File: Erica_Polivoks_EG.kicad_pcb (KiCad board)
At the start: 2 copper layers, 81.7 x 128.5 mm, 105 parts, among them J1 GATE IN, J2 INV EG OUT, J3 Eurorack_Power_10pin_Unshroud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, J4 GATE D.OUT, J5 EG OUT, Q1 4, Q2 4, Q3 4, Q4 4, Q5 4, Q6 4, Q7 6, Q8 6, Q9 6, U1 TL074

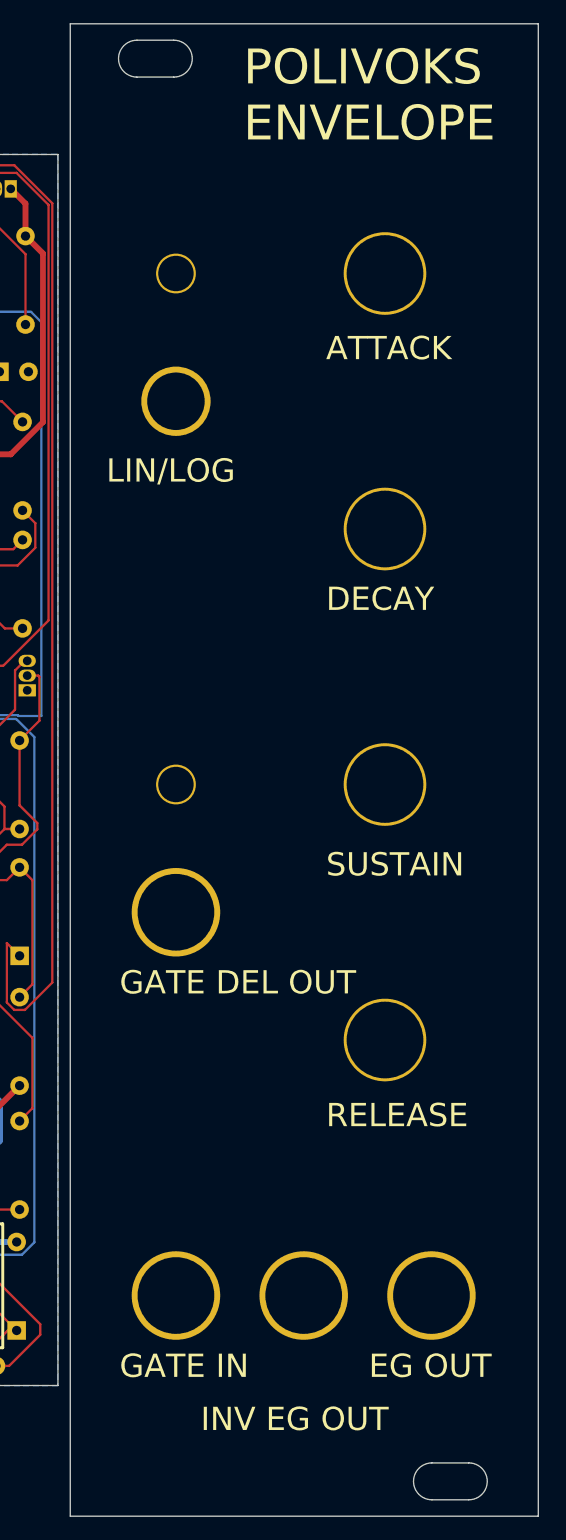
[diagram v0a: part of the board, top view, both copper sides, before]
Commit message: broke panel out into separate PCB file
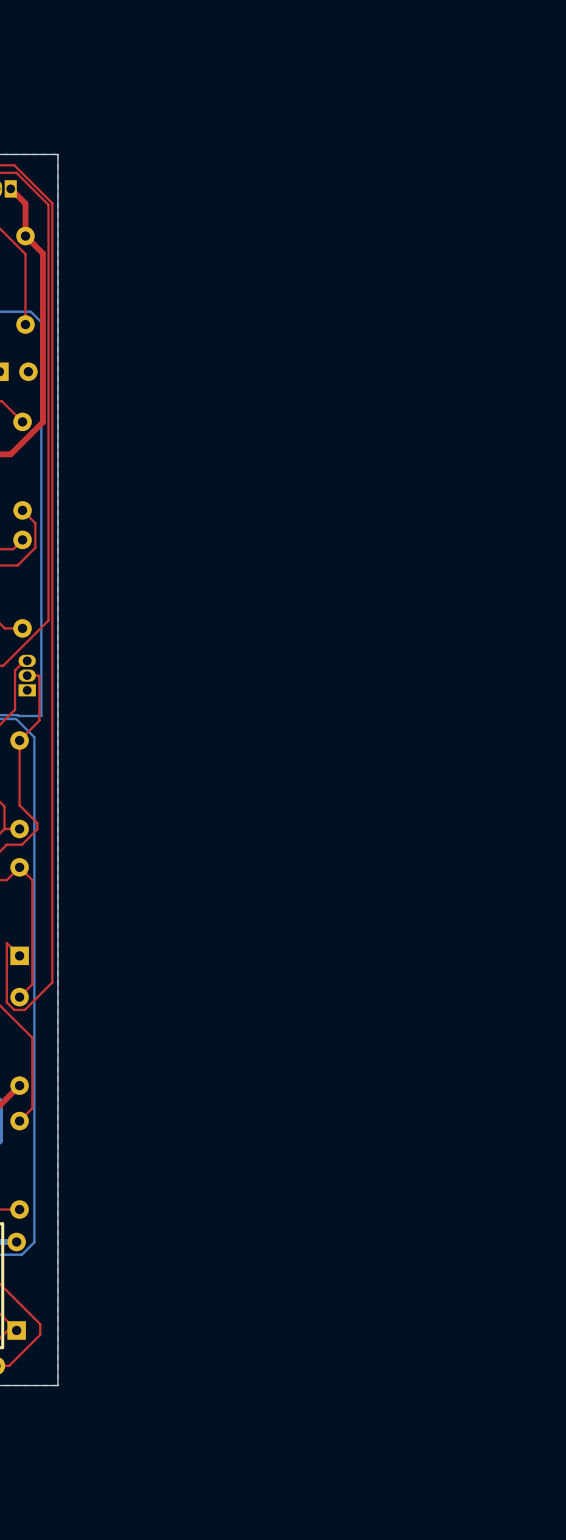
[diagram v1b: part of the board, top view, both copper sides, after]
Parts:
- removed REF** (x4): GND, PCM_4ms_Faceplate:Faceplate_Hole_Jack_3.5mm
- removed REF** (x2): Faceplate_Hole_LED_3mm, PCM_4ms_Faceplate:Faceplate_Hole_LED_3mm
- removed REF** (x4): Faceplate_Hole_Pot_9mm, PCM_4ms_Faceplate:Faceplate_Hole_Pot_9mm
- removed REF** (x2): Rail_mount_slot, PCM_4ms_Faceplate:Faceplate_Rail_Mount_Slot
- removed REF**: Faceplate_Hole_SubMini_Toggle, PCM_4ms_Faceplate:Faceplate_Hole_SubMini_Toggle
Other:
- board size 81.7 x 128.5 mm -> 40.3 x 106 mm
- board text removed: "EG OUT"
- board text removed: "GATE DEL OUT"
- board text removed: "GATE IN"
- board text removed: "INV EG OUT"
- board text removed: "LIN/LOG"
- board text removed: "POLIVOKS ENVELOPE"

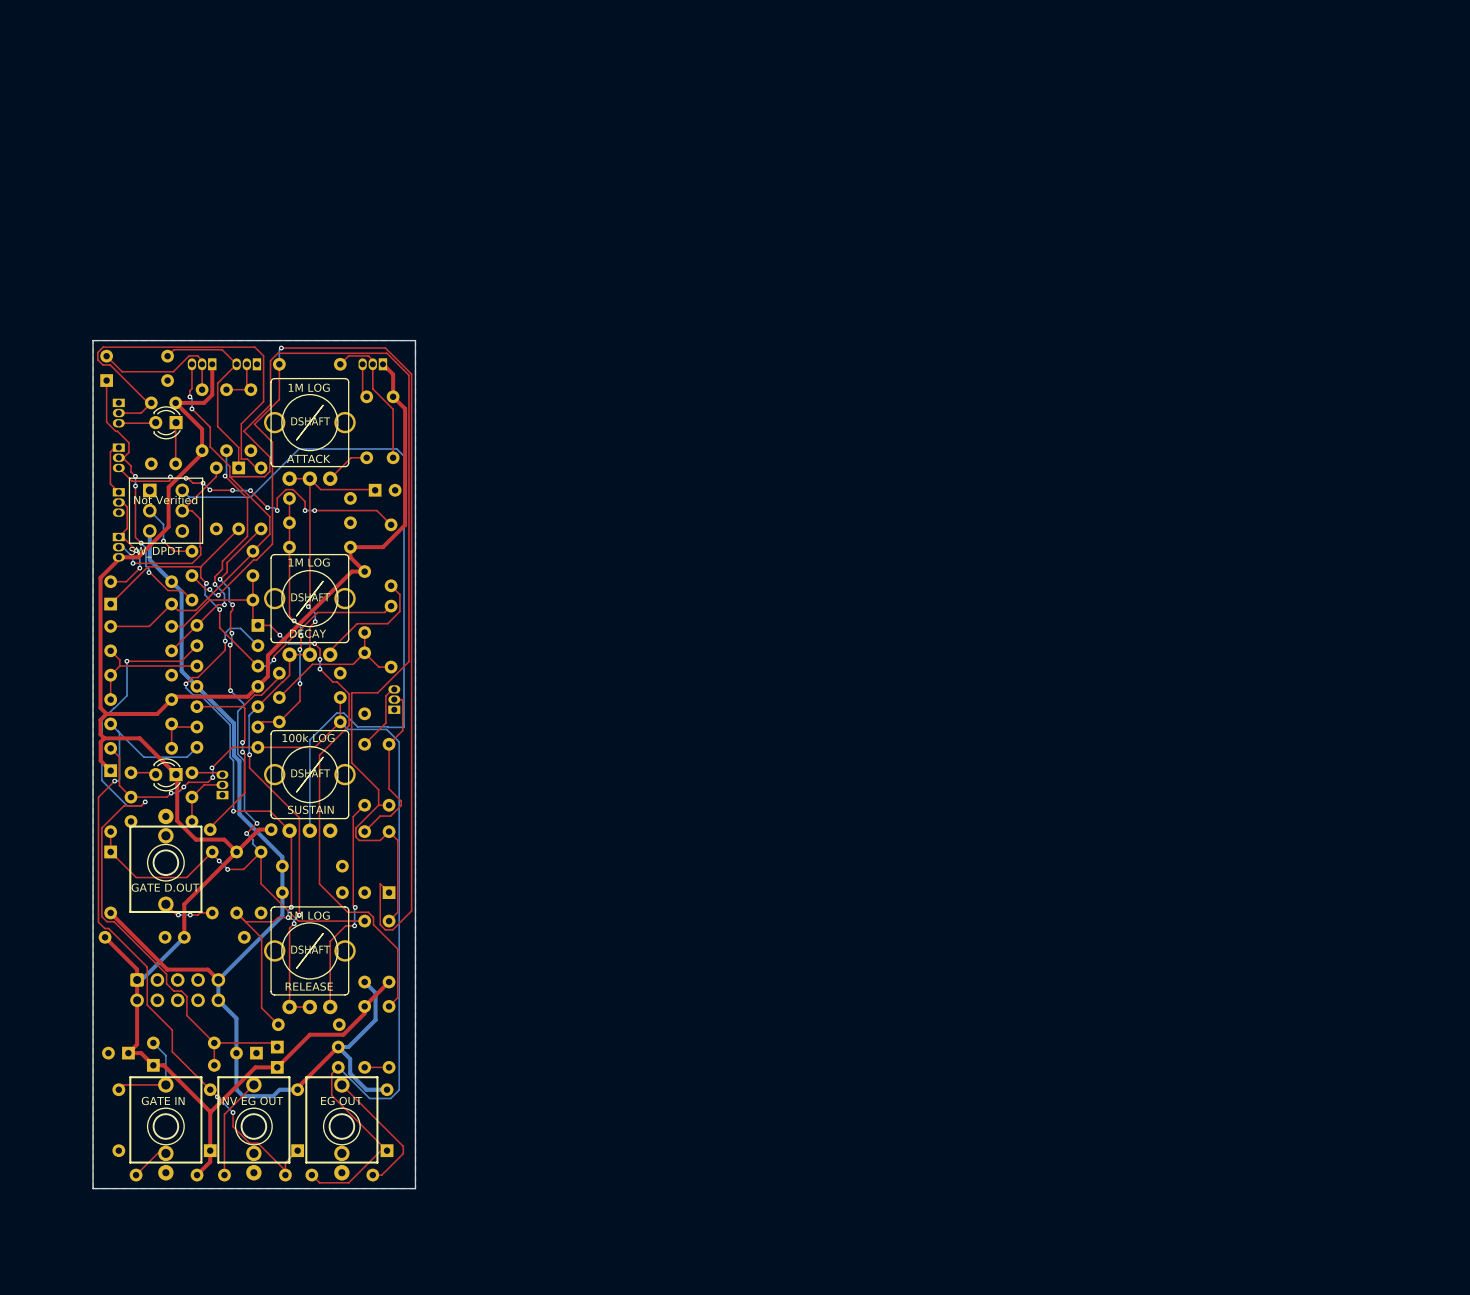
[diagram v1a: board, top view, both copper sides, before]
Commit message: fixed silkscreening issues - just 'not verified' text issue remains
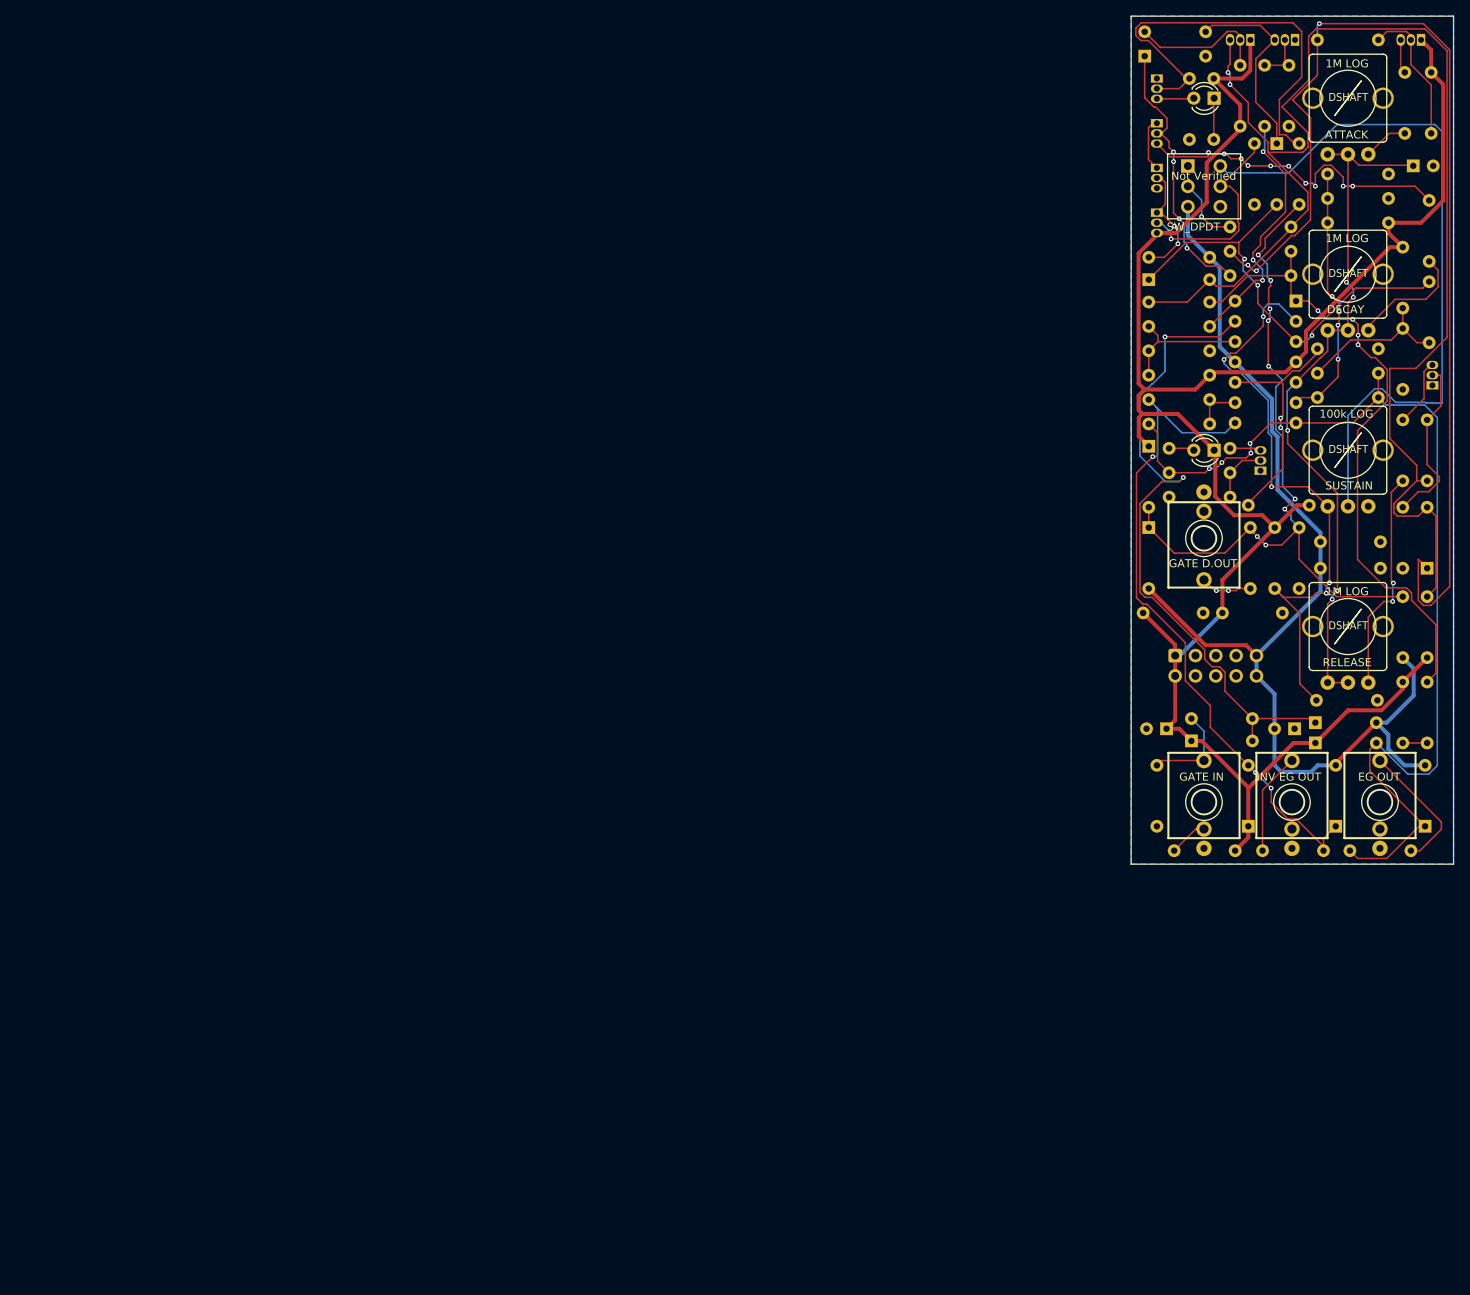
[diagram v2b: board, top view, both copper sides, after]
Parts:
- C4: value 47uF -> <47uF
- R46: value 3.3k -> 3.3
- R47: value 100k -> 100
- R5: value 100k -> <100k
- moved C3 135.9 mm to (201.6, 96.1)
- moved D3 135.9 mm to (208.4, 37.4)
- moved Q5 135.9 mm to (227.8, 67.6)
- moved R10 135.9 mm to (206.8, 27.6)
- moved R49 135.9 mm to (222.3, 47.3)
- moved C1 135.9 mm to (191.7, 96.1)
- moved C2 135.9 mm to (194.6, 110.6)
- moved C4 135.9 mm to (210.6, 110.6)
- moved C5 135.9 mm to (221.3, 87.2)
- moved C6 135.9 mm to (221.3, 90.5)
- moved C7 135.9 mm to (225.4, 40.2)
- moved D1 135.9 mm to (213.2, 109.8)
- moved D11 135.9 mm to (199.3, 31.8)
- moved D12 135.9 mm to (192.4, 85.4)
- moved D13 135.9 mm to (192.4, 75.3)
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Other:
- board text added: "k"

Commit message: almost ready to go
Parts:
- moved C1 123.1 mm to (79.6, 146.9)
- moved C2 123.1 mm to (82.5, 161.4)
- moved C3 123.1 mm to (89.5, 146.9)
- moved C7 123.1 mm to (113.3, 91.0)
- moved D1 123.1 mm to (101.1, 160.6)
- moved D11 123.1 mm to (87.2, 82.5)
- moved D12 123.1 mm to (80.3, 136.2)
- moved D13 123.1 mm to (80.3, 126.1)
- moved D15 123.1 mm to (101.1, 163.1)
- moved D18 123.1 mm to (87.2, 126.5)
- moved D2 123.1 mm to (85.6, 162.9)
- moved D3 123.1 mm to (96.3, 88.2)
- moved D4 123.1 mm to (115.1, 141.3)
- moved D5 123.1 mm to (80.3, 105.2)
- moved D8 123.1 mm to (92.7, 173.6)
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
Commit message: waiting for DPDT switch to measure - otherwise complete
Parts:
- C2: value 47uF -> ◀47uF
- C4: value <47uF -> ◀47uF
- C7: value 4.7uF -> ◀4.7uF
- D11: value GATE DELAY (YELLOW LED) -> GATE DELAY
- D18: value EG OUT (YELLOW LED) -> EG OUT
- Q2: value 4 -> 4▼
- Q3, Q4, Q6: value 4 -> ◀4
- Q7, Q8: value 6 -> 6▼
- Q9: value 6 -> ◀6
- R5: value <100k -> ◀100k
- moved J4 34.7 mm to (59.9, 116.0)
- moved C5 34.7 mm to (82.0, 116.5)
- moved D3 34.7 mm to (69.0, 66.7)
- moved D7 34.7 mm to (76.4, 152.1)
- moved Q2 34.7 mm to (71.3, 53.8)
- moved Q5 34.7 mm to (88.5, 96.9)
- moved R10 34.7 mm to (67.5, 56.9)
- moved R11 34.7 mm to (70.5, 64.6)
- moved R33 34.7 mm to (74.1, 92.4)
- moved R37 34.7 mm to (74.8, 155.1)
- moved R45 34.7 mm to (74.1, 98.5)
- moved R47 34.7 mm to (63.2, 110.9)
- moved R48 34.7 mm to (63.2, 107.9)
- moved R49 34.7 mm to (83.0, 76.6)
- moved C2 34.7 mm to (55.2, 139.9)
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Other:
- board text added: "JLCJLCJLCJLC"
- board text added: "LED"
- board text added: "PCB BY 42 BERLIN SYNTHLAB"
- board text added: "POLIVOKS EG 2 BY ERICA SYNTHS -"
- board text added: "SynthLab"
- board text added: "V1.0"
- board text added: "github.com/fablabnk/SynthLabProjects"

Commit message: v1.0 ready for production
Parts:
- removed SW_DPDT: SW_DPDT_x2, PCM_4ms_Switch:Switch_Toggle_DPDT_SubMini
- added SW1: SW_DPDT_x2, Library:Switch_Toggle_DPDT_MS202, F.Cu at (60.1, 72.0)
- C1, C3, C5, C6: value 104 -> 0.1uF
- C2, C4: value ◀47uF -> 47uFx25V
- C7: value ◀4.7uF -> 4.7uFx16V
- D1, D12, D13, D14, D15, D2, D3, D4, D5, D6, D7, D8: value 4148 -> 1N4148
- D11: value GATE DELAY -> LED
- D18: value EG OUT -> LED
- J4: value GATE D.OUT -> GATE DELAY OUT
- Q1, Q5: value 4 -> 2N3904
- Q2: value 4▼ -> 2N3904
- Q3, Q4, Q6: value ◀4 -> 2N3904
- Q7, Q8: value 6▼ -> 2N3906
- Q9: value ◀6 -> 2N3906
- R46: value 3.3 -> 3.3k
- R47: value 100 -> 100k
- R5: value ◀100k -> 100k
- moved R19 2.24 mm to (73.0, 77.1)
- moved R38 0.89 mm to (58.1, 57.7)
- moved R40 0.89 mm to (61.1, 57.7)
- moved D6 0.51 mm to (52.5, 55.3)
- moved D7 0.38 mm to (76.2, 152.4)
- moved R12 0.25 mm to (52.5, 52.5)
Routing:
- net Net-(Q4-B): track 52.9 -> 27.5 mm, vias 0 -> 1
- net Net-(SW1B-A): track 90.1 -> 65.2 mm, vias 0 -> 9
- net Net-(D6-K): track 34.8 -> 49.0 mm, vias 4 -> 0
- net Net-(D3-A): track 55.4 -> 69.2 mm, vias 3 -> 6
- net Net-(R10-Pad2): track 31.7 -> 45.4 mm
- net Net-(Q6-B): track 26.3 -> 17.1 mm, vias 1 -> 0
- net Net-(D4-K): track 137.1 -> 131.9 mm, vias 3 -> 1
- net Net-(Q3-C): track 41.4 -> 37.0 mm, vias 10 -> 2
- net Net-(Q6-E): track 15.1 -> 12.5 mm, vias 2 -> 0
- net +12V: track 259.8 -> 262.3 mm
- net Net-(U1C-+): track 29.8 -> 32.0 mm
- net Net-(D4-A): track 175.0 -> 173.0 mm, vias 2 -> 4
- net -12V: track 134.6 -> 132.7 mm
- net Net-(SW1A-B): track 8.59 -> 9.68 mm, vias 1 -> 0
- net Net-(D11-A): track 5.18 -> 4.29 mm
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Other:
- board text added: "▶"
- board text removed: "LED"
- board text removed: "k"

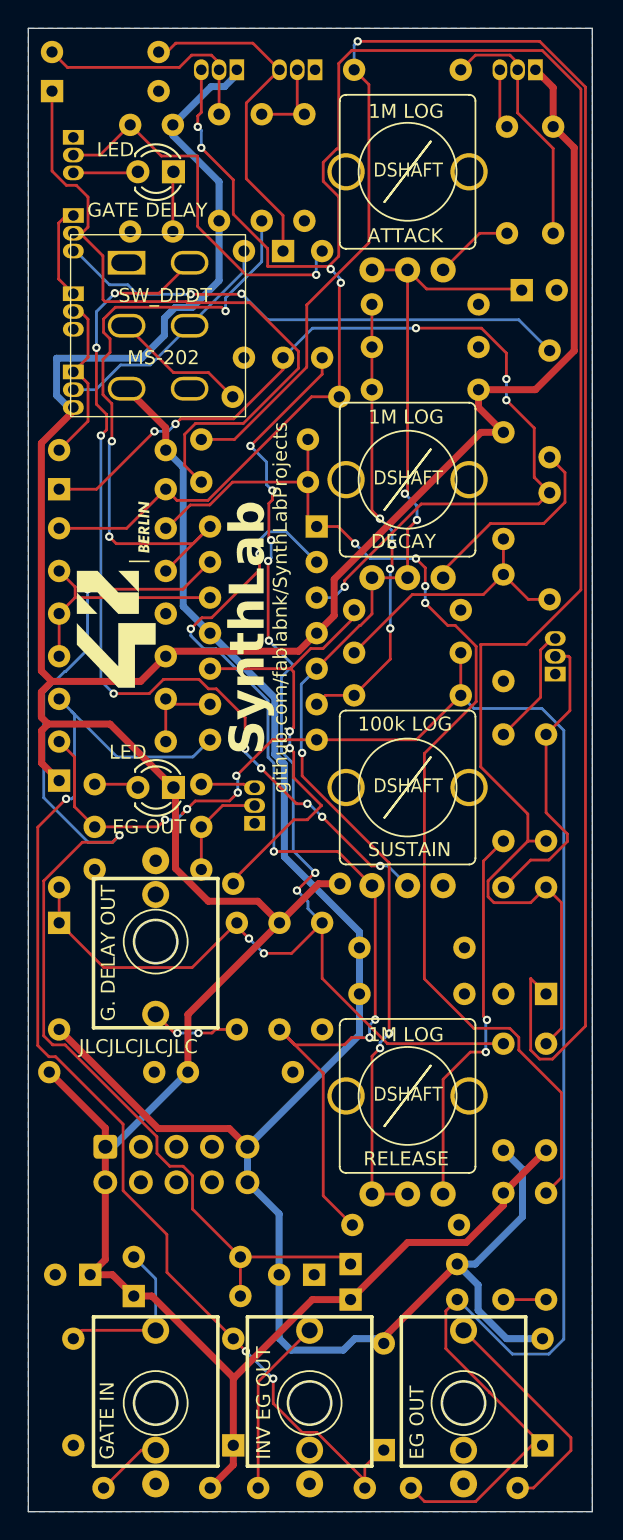
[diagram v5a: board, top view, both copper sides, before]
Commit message: v1.0 ready for production - added actual HP-size outli]ne on User.Dawings layer
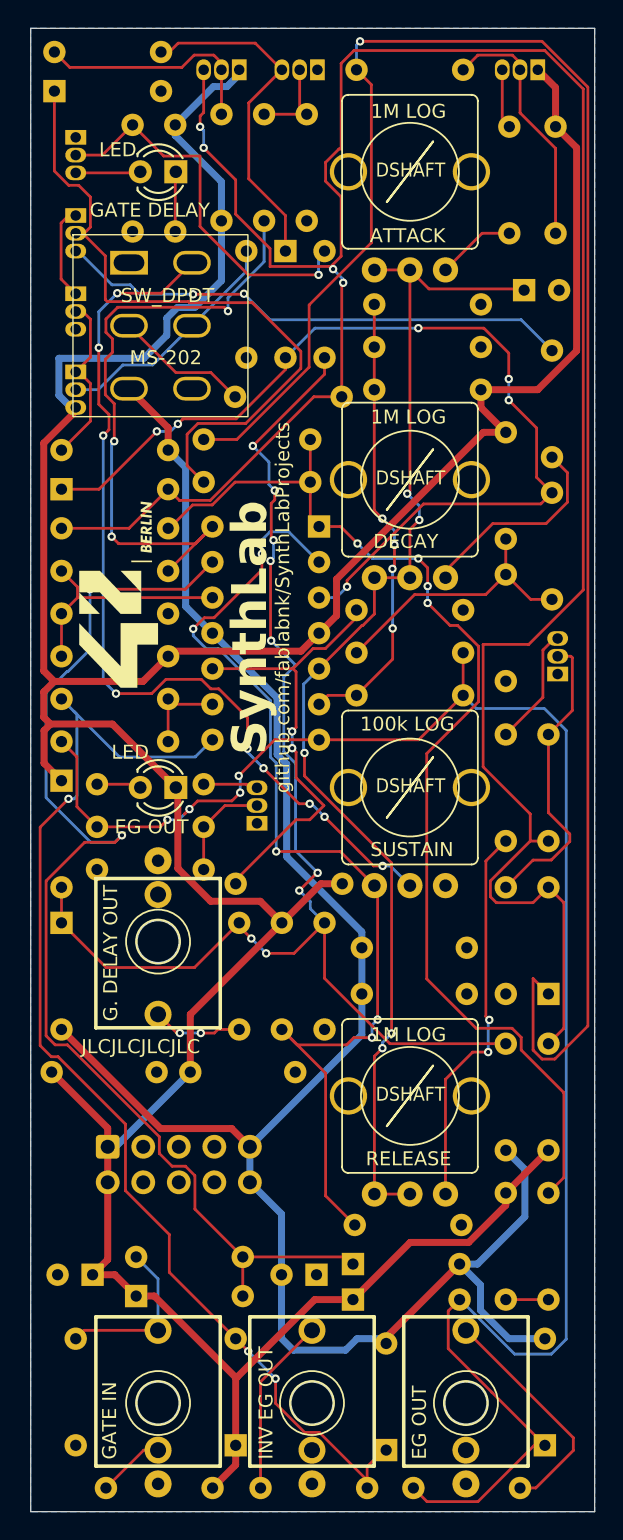
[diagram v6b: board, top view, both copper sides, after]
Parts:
- moved C1 0.17 mm to (52.5, 125.4)
- moved C3 0.17 mm to (62.4, 125.4)
- moved C4 0.17 mm to (71.4, 139.9)
- moved C5 0.17 mm to (82.1, 116.5)
- moved C6 0.17 mm to (82.1, 119.8)
- moved C7 0.17 mm to (86.2, 69.5)
- moved D1 0.17 mm to (74.0, 139.1)
- moved D11 0.17 mm to (60.1, 61.0)
- moved D12 0.17 mm to (53.2, 114.7)
- moved D13 0.17 mm to (53.2, 104.6)
- moved D14 0.17 mm to (87.7, 152.1)
- moved D15 0.17 mm to (74.0, 141.6)
- moved D18 0.17 mm to (60.1, 105.0)
- moved D3 0.17 mm to (69.2, 66.7)
- moved D4 0.17 mm to (88.0, 119.8)
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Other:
- board text added: "▲"

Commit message: most of V1.1 changes completed
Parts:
- C1, C3, C5, C6: footprint Capacitor_THT:C_Axial_L3.8mm_D2.6mm_P7.50mm_Horizontal -> Capacitor_THT:C_Disc_D3.0mm_W1.6mm_P2.50mm
- Q1, Q2, Q3, Q4, Q5, Q6, Q7, Q8, Q9: footprint Package_TO_SOT_THT:TO-92_Inline -> Library:TO-92L_Inline_Wider
- R34: value NU 39K -> NU 39K
- RV1, RV2, RV3: value 1M LOG -> 1M A
- RV4: value 100k LOG -> 100k A
- moved C5 1.29 mm to (81.2, 115.6)
- moved C6 0.99 mm to (81.2, 119.4)
- moved C1 0.75 mm to (53.2, 125.5)
- moved C3 0.09 mm to (62.4, 125.5)
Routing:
- net -12V: track 132.7 -> 139.4 mm
- net Net-(Q6-B): track 17.1 -> 23.7 mm
- net +12V: track 262.3 -> 259.6 mm
- net Net-(D7-K): track 84.2 -> 86.4 mm
- net Net-(D1-K): track 84.1 -> 85.9 mm
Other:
- board text added: "V1.1"
- board text removed: "V1.0"
